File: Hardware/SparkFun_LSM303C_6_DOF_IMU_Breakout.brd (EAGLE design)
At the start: 25.4 x 25.4 mm, 27 parts, among them Q1 2.5A/30V, U1 LSM303C, U2 LM3880

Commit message: Silk work
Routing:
- net GND: vias 10 -> 9
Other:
- board text added: "!CS_XL!"
- board text added: "SJ4"
- board text removed: "PWR SHORT"
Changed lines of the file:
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@@
 <setting verticaltext="up"/>
 </settings>
-<grid distance="0.01" unitdist="inch" unit="inch" style="lines" multiple="1" display="yes" altdistance="0.001" altunitdist="inch" altunit="inch"/>
+<grid distance="0.001" unitdist="inch" unit="inch" style="lines" multiple="1" display="yes" altdistance="0.001" altunitdist="inch" altunit="inch"/>
 <layers>
-<layer number="1" name="Top" color="4" fill="1" visible="no" active="yes"/>
+<layer number="1" name="Top" color="4" fill="1" visible="yes" active="yes"/>
 <layer number="2" name="Route2" color="1" fill="3" visible="no" active="no"/>
 <layer number="3" name="Route3" color="4" fill="3" visible="no" active="no"/>
@@
 <layer number="19" name="Unrouted" color="6" fill="1" visible="yes" active="yes"/>
 <layer number="20" name="Dimension" color="15" fill="1" visible="yes" active="yes"/>
-<layer number="21" name="tPlace" color="16" fill="1" visible="no" active="yes"/>
+<layer number="21" name="tPlace" color="16" fill="1" visible="yes" active="yes"/>
 <layer number="22" name="bPlace" color="14" fill="1" visible="yes" active="yes"/>
-<layer number="23" name="tOrigins" color="15" fill="1" visible="no" active="yes"/>
+<layer number="23" name="tOrigins" color="15" fill="1" visible="yes" active="yes"/>
 <layer number="24" name="bOrigins" color="15" fill="1" visible="yes" active="yes"/>
 <layer number="25" name="tNames" color="7" fill="1" visible="no" active="yes"/>
@@
 <layer number="27" name="tValues" color="7" fill="1" visible="no" active="yes"/>
 <layer number="28" name="bValues" color="7" fill="1" visible="no" active="yes"/>
-<layer number="29" name="tStop" color="7" fill="3" visible="no" active="yes"/>
+<layer number="29" name="tStop" color="7" fill="3" visible="yes" active="yes"/>
 <layer number="30" name="bStop" color="7" fill="6" visible="no" active="yes"/>
 <layer number="31" name="tCream" color="7" fill="4" visible="no" active="yes"/>
@@
 <layer number="49" name="Reference" color="7" fill="1" visible="yes" active="yes"/>
 <layer number="50" name="dxf" color="7" fill="1" visible="no" active="yes"/>
-<layer number="51" name="tDocu" color="6" fill="1" visible="no" active="yes"/>
-<layer number="52" name="bDocu" color="7" fill="1" visible="yes" active="yes"/>
+<layer number="51" name="tDocu" color="6" fill="1" visible="yes" active="yes"/>
+<layer number="52" name="bDocu" color="7" fill="1" visible="no" active="yes"/>
 <layer number="53" name="tGND_GNDA" color="7" fill="9" visible="no" active="no"/>
 <layer number="54" name="bGND_GNDA" color="1" fill="9" visible="no" active="no"/>
@@
 <text x="22.733" y="1.27" size="0.8128" layer="21" font="vector" ratio="15" align="center-right">INT_MAG</text>
 <text x="22.733" y="16.51" size="0.8128" layer="21" font="vector" ratio="15" align="center-right">SCL/SCLK</text>
-<text x="22.733" y="9.652" size="0.8128" layer="21" font="vector" ratio="15" align="center-right">!CS_XL</text>
+<text x="22.733" y="9.652" size="0.8128" layer="21" font="vector" ratio="15" align="center-right">!CS_XL!</text>
 <text x="22.733" y="3.81" size="0.8128" layer="21" font="vector" ratio="15" align="center-right">!CS_MAG</text>
 <text x="22.733" y="19.05" size="0.8128" layer="21" font="vector" ratio="15" align="center-right">SDA/SDI/SDO</text>
@@
 <text x="3.048" y="6.35" size="0.8128" layer="22" ratio="15" rot="MR180" align="center-left">MAG</text>
 <text x="4.6482" y="9.144" size="0.8128" layer="22" ratio="15" rot="MR0" align="center-left">P/U</text>
-<wire x1="21.336" y1="7.112" x2="19.939" y2="6.731" width="0.1778" layer="21"/>
+<wire x1="21.336" y1="7.112" x2="20.4216" y2="6.858" width="0.1778" layer="21"/>
 <wire x1="21.336" y1="7.112" x2="21.209" y2="6.858" width="0.1778" layer="21"/>
 <wire x1="21.209" y1="6.858" x2="21.082" y2="7.239" width="0.1778" layer="21"/>
 <wire x1="21.082" y1="7.239" x2="21.336" y2="7.112" width="0.1778" layer="21"/>
-<text x="11.938" y="5.207" size="0.8128" layer="21" ratio="15" align="center-left">PWR SHORT</text>
+<text x="17.0688" y="5.2324" size="0.8128" layer="21" ratio="15" align="center-left">SJ4</text>
 <dimension x1="0" y1="0" x2="25.4" y2="0" x3="12.7" y3="-3.81" textsize="1.778" textratio="15" layer="47" unit="inch"/>
 <dimension x1="25.4" y1="0" x2="25.4" y2="25.4" x3="29.21" y3="12.7" textsize="1.778" textratio="15" layer="47" unit="inch"/>
@@
 <wire x1="10.4648" y1="15.4432" x2="10.8712" y2="15.0368" width="0.127" layer="22"/>
 <wire x1="10.4648" y1="15.0368" x2="10.8712" y2="15.4432" width="0.127" layer="22"/>
-<wire x1="19.939" y1="6.731" x2="18.669" y2="5.588" width="0.1778" layer="21" curve="60"/>
+<wire x1="20.4216" y1="6.858" x2="19.2024" y2="5.6134" width="0.1778" layer="21" curve="60"/>
 </plain>
 <attributes>
@@
 <wire x1="11.934" y1="8.894" x2="11.164" y2="8.894" width="0.254" layer="1"/>
 <via x="20.828" y="12.7" extent="1-16" drill="0.508"/>
-<via x="20.828" y="10.414" extent="1-16" drill="0.508"/>
 <via x="20.574" y="7.62" extent="1-16" drill="0.508"/>
 <wire x1="20.828" y1="10.414" x2="20.828" y2="7.874" width="0.254" layer="1"/>
@@
 <wire x1="8.128" y1="13.716" x2="8.128" y2="10.668" width="0.254" layer="16"/>
 <contactref element="R2" pad="1"/>
-<wire x1="5.842" y1="14.185" x2="6.389" y2="14.185" width="0.254" layer="1"/>
-<wire x1="6.389" y1="14.185" x2="7.366" y2="13.208" width="0.254" layer="1"/>
-<wire x1="7.366" y1="13.208" x2="7.366" y2="11.43" width="0.254" layer="1"/>
+<wire x1="5.842" y1="14.185" x2="6.4398" y2="14.185" width="0.254" layer="1"/>
+<wire x1="6.4398" y1="14.185" x2="7.366" y2="13.2588" width="0.254" layer="1"/>
+<wire x1="7.366" y1="13.2588" x2="7.366" y2="11.43" width="0.254" layer="1"/>
 <wire x1="7.366" y1="11.43" x2="8.128" y2="10.668" width="0.254" layer="1"/>
 </signal>

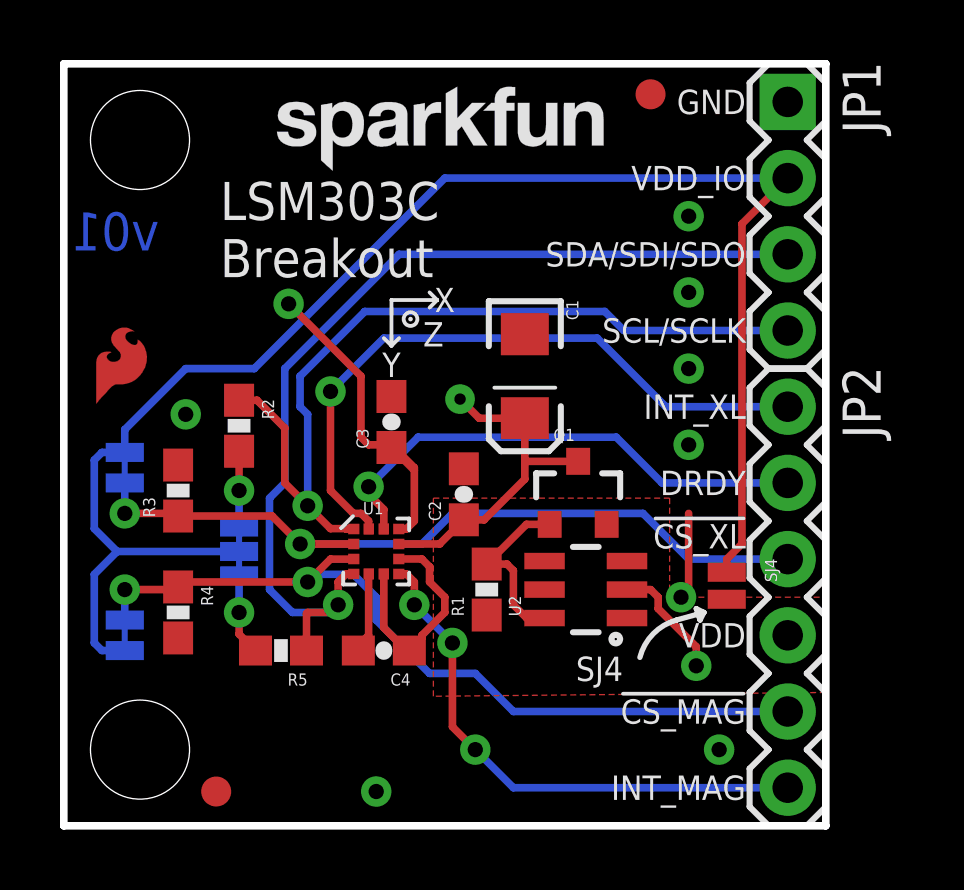
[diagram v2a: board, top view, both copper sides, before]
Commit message: Closed VDD-VDD_IO jumper making the PCBA single input volatage (3.3V) by default
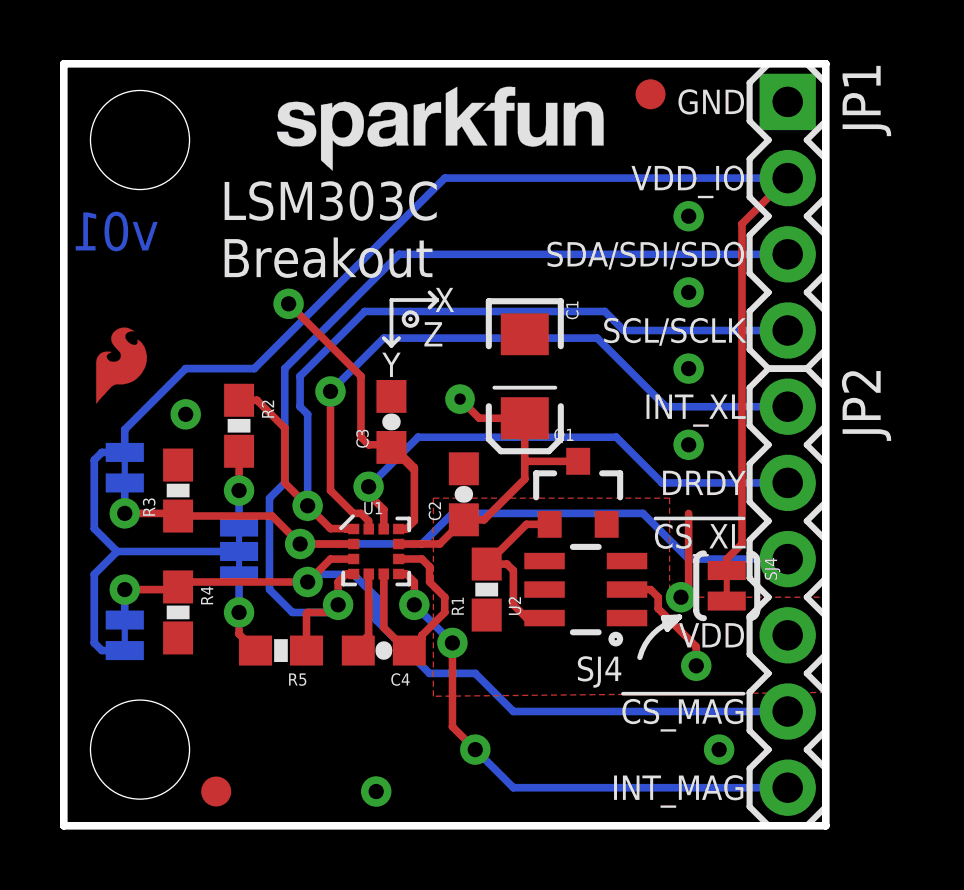
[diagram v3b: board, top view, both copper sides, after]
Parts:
- SJ4: value JUMPER-PAD-2-NO -> JUMPER-PAD-2-NC_BY_TRACE; device SparkFun-Passives:PAD-JUMPER-2-NO_NO_SILK -> SparkFun-Passives:PAD-JUMPER-2-NC_BY_TRACE_YES_SILK
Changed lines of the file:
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@@
 <layer number="27" name="tValues" color="7" fill="1" visible="no" active="yes"/>
 <layer number="28" name="bValues" color="7" fill="1" visible="no" active="yes"/>
-<layer number="29" name="tStop" color="7" fill="3" visible="yes" active="yes"/>
+<layer number="29" name="tStop" color="7" fill="3" visible="no" active="yes"/>
 <layer number="30" name="bStop" color="7" fill="6" visible="no" active="yes"/>
 <layer number="31" name="tCream" color="7" fill="4" visible="no" active="yes"/>
@@
 <text x="3.048" y="6.35" size="0.8128" layer="22" ratio="15" rot="MR180" align="center-left">MAG</text>
 <text x="4.6482" y="9.144" size="0.8128" layer="22" ratio="15" rot="MR0" align="center-left">P/U</text>
-<wire x1="21.336" y1="7.112" x2="20.4216" y2="6.858" width="0.1778" layer="21"/>
-<wire x1="21.336" y1="7.112" x2="21.209" y2="6.858" width="0.1778" layer="21"/>
-<wire x1="21.209" y1="6.858" x2="21.082" y2="7.239" width="0.1778" layer="21"/>
-<wire x1="21.082" y1="7.239" x2="21.336" y2="7.112" width="0.1778" layer="21"/>
+<wire x1="20.5232" y1="6.9596" x2="20.4216" y2="6.858" width="0.1778" layer="21"/>
+<wire x1="20.4216" y1="6.858" x2="20.1168" y2="6.5532" width="0.1778" layer="21"/>
+<wire x1="20.1168" y1="6.5532" x2="19.9898" y2="6.9342" width="0.1778" layer="21"/>
+<wire x1="19.9898" y1="6.9342" x2="20.5232" y2="6.9596" width="0.1778" layer="21"/>
 <text x="17.0688" y="5.2324" size="0.8128" layer="21" ratio="15" align="center-left">SJ4</text>
 <dimension x1="0" y1="0" x2="25.4" y2="0" x3="12.7" y3="-3.81" textsize="1.778" textratio="15" layer="47" unit="inch"/>
@@
 <element name="JP1" library="SparkFun-Connectors" package="1X04" value="" x="24.13" y="24.13" rot="R270"/>
 <element name="SJ1" library="SparkFun-Passives" package="PAD-JUMPER-3-3OF3_NC_BY_TRACE_YES_SILK_FULL_BOX" value="" x="5.842" y="9.144" rot="MR90"/>
-<element name="SJ4" library="SparkFun-Passives" package="PAD-JUMPER-2-NO_NO_SILK" value="JUMPER-PAD-2-NO" x="22.098" y="8.001" rot="R270"/>
+<element name="SJ4" library="SparkFun-Passives" package="PAD-JUMPER-2-NC_BY_TRACE_YES_SILK" value="JUMPER-PAD-2-NC_BY_TRACE" x="22.098" y="8.001" rot="R270"/>
 <element name="TP1" library="SparkFun-Passives" package="TP_15TH" value="VDD_TP" x="13.208" y="14.224"/>
 <element name="STANDOFF1" library="SparkFun-Electromechanical" package="STAND-OFF" value="STAND-OFF" x="2.54" y="22.86"/>
@@
 <via x="7.493" y="17.399" extent="1-16" drill="0.508"/>
 <wire x1="7.493" y1="17.399" x2="8.001" y2="16.891" width="0.254" layer="16"/>
-<wire x1="22.098" y1="8.451" x2="22.098" y2="8.89" width="0.254" layer="1"/>
+<wire x1="22.098" y1="8.509" x2="22.098" y2="8.89" width="0.254" layer="1"/>
 <wire x1="22.098" y1="8.89" x2="22.606" y2="9.398" width="0.254" layer="1"/>
 <wire x1="22.606" y1="9.398" x2="22.606" y2="20.066" width="0.254" layer="1"/>

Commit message: Fixed logic inversion bug and simplified board by removing jumpers
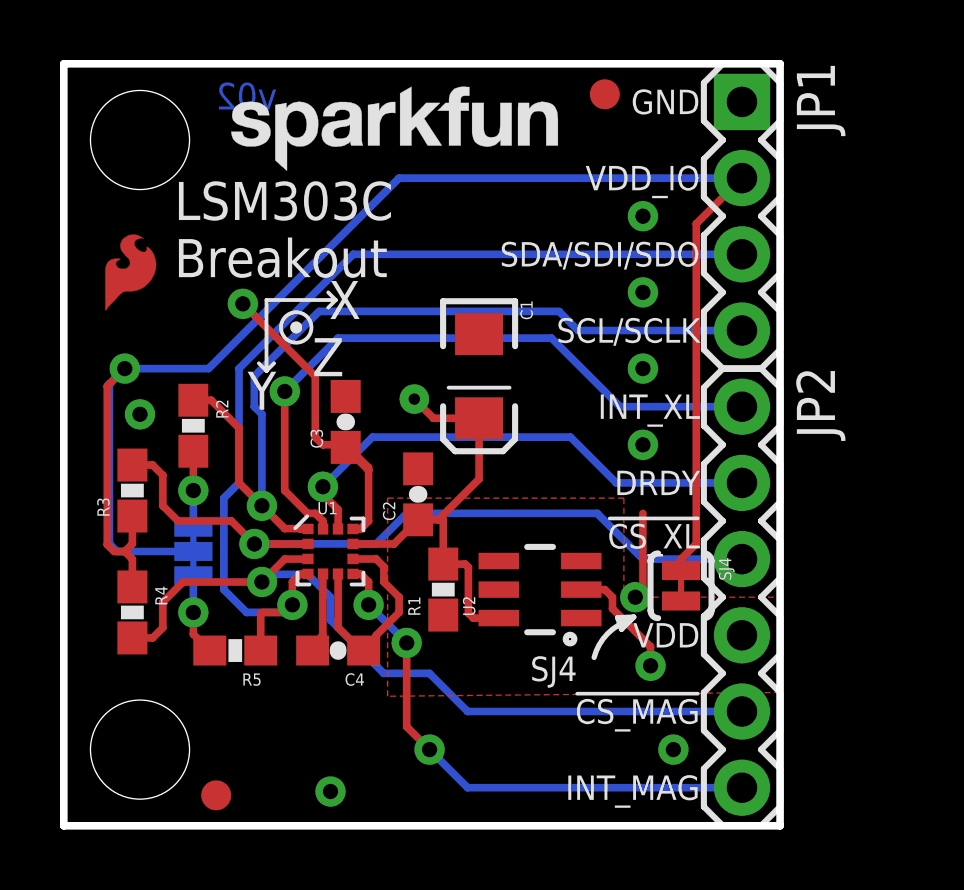
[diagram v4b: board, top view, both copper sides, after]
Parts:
- removed Q1: 2.5A/30V, SparkFun-DiscreteSemi:SOT23-3
- removed SJ2, SJ3: JUMPER-PAD-2-NC_BY_TRACE, SparkFun-Passives:PAD-JUMPER-2-NC_BY_TRACE_YES_SILK
- FRAME1: value (none) -> FRAME-LETTER
- R1: value 100k -> 68
- moved LOGO2 3.11 mm to (1.07, 16.8)
- moved C1 1.52 mm to (13.8, 15.0)
- moved C2 1.52 mm to (11.8, 11.0)
- moved C3 1.52 mm to (9.40, 13.5)
- moved FID1 1.52 mm to (18.0, 24.4)
- moved TP1 1.52 mm to (11.7, 14.2)
- moved U2 1.52 mm to (15.9, 7.87)
- moved LOGO1 1.52 mm to (5.08, 21.3)
- moved R2 1.52 mm to (4.32, 13.3)
- moved R3 1.52 mm to (2.29, 11.2)
- moved R4 1.52 mm to (2.29, 7.11)
- moved R5 1.52 mm to (5.71, 5.84)
- moved SJ1 1.52 mm to (4.32, 9.14)
- moved C4 1.52 mm to (9.14, 5.84)
- moved U$8 1.52 mm to (14.4, 7.75)
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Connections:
- removed net N$3: Q1.1, R1.2, U2.6
- net !CS_MAG: now also R4.2; no longer R4.1, SJ3.2
- net !CS_XL: now also R3.2; no longer R3.1, SJ2.2
- net GND: no longer R3.2, R4.2
- net VCC: no longer Q1.2
- net VDD: now also R1.2, U2.6; no longer Q1.3
- net VDD_IO: now also R3.1, R4.1; no longer SJ2.1, SJ3.1
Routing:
- net N$3: track 5.99 -> 0.00 mm
- net VDD: track 11.3 -> 14.7 mm
- net VDD_IO: track 65.4 -> 67.6 mm, vias 1 -> 2
- net !CS_MAG: track 27.5 -> 25.9 mm, vias 2 -> 1
- net !CS_XL: track 26.4 -> 24.8 mm, vias 2 -> 1
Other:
- board size 25.4 x 25.4 mm -> 23.9 x 25.4 mm
- board text added: ">VERSION"

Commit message: Small tweaks
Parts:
- moved SJ4 0.15 mm to (20.4, 8.00)
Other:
- board text added: "I2C"
- board text removed: "MAG"
- board text removed: "XL"

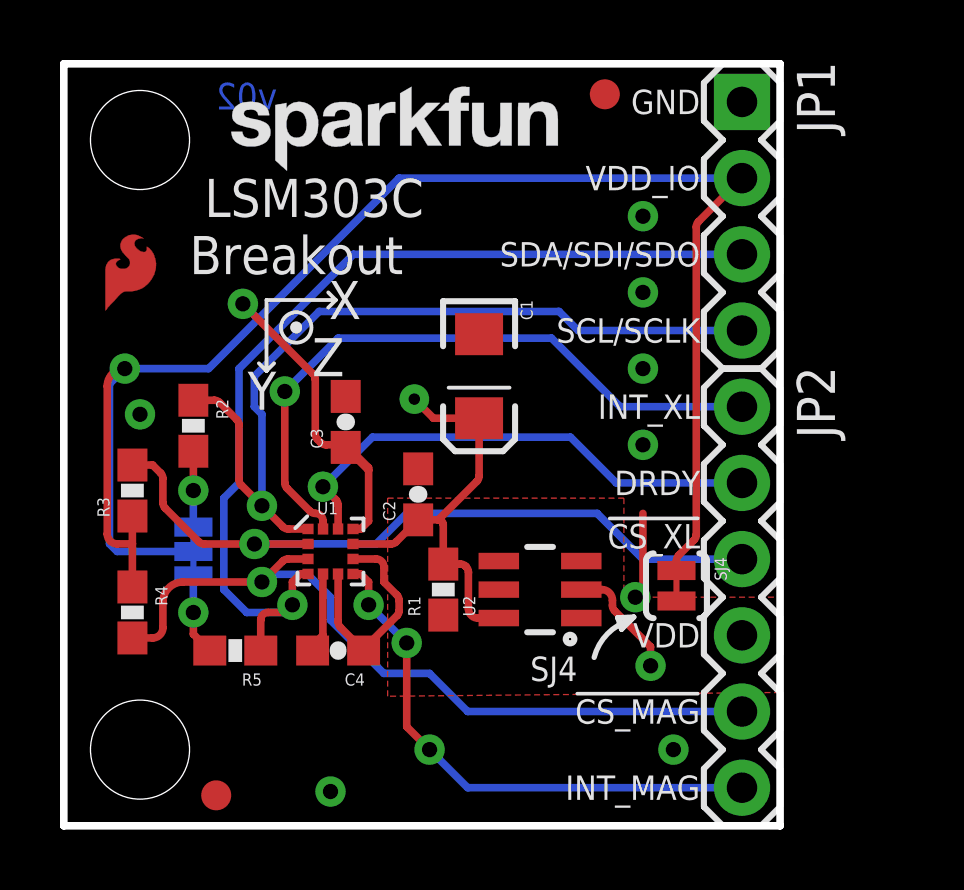
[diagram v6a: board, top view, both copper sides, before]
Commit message: Fixed 'width' dimension
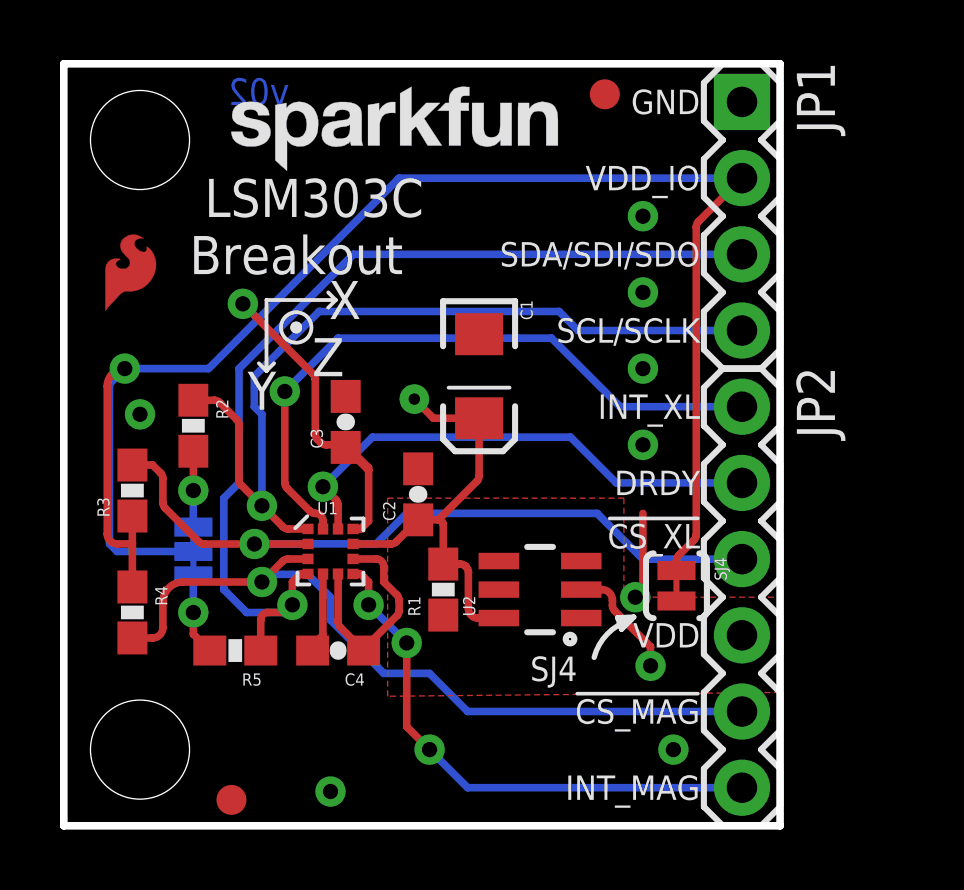
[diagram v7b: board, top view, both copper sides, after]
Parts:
- moved FID2 0.53 mm to (5.59, 0.86)
